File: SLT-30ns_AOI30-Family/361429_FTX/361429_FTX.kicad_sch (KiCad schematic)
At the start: 5 parts, among them T1 IBM_Transistor, T2 IBM_Transistor, T3 IBM_Transistor, T4 IBM_Transistor, U1 12-Pin_SLx_Can

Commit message: Bunch of schematics.
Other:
- note added: "All Transistors ACA"
- note removed: "All Transistors DC"
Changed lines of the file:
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@@
     (stroke (width 0) (type default) (color 0 0 0 0))
   )
-  (text "All Transistors DC" (at 118.11 101.6 0)
+  (text "All Transistors ACA" (at 118.11 101.6 0)
     (effects (font (size 1.27 1.27)) (justify left bottom))
   )
@@
     (pin "3")
   )
+  (symbol (lib_id "IBM_SLT-SLD:IBM_Transistor") (at 165.1 128.27 0) (unit 1)
+    (in_bom yes) (on_board yes) (fields_autoplaced)
+    (property "Reference" "T3" (id 0) (at 168.91 127.6349 0)
+      (effects (font (size 1.27 1.27)) (justify left))
+    )
+    (property "Value" "IBM_Transistor" (id 1) (at 168.91 130.1749 0)
+      (effects (font (size 1.27 1.27)) (justify left))
+    )
+    (property "Footprint" "" (id 2) (at 165.1 128.27 0)
+      (effects (font (size 1.27 1.27)) hide)
+    )
+    (property "Datasheet" "" (id 3) (at 165.1 128.27 0)
+      (effects (font (size 1.27 1.27)) hide)
+    )
+    (pin "1")
+    (pin "2")
+    (pin "3")
+  )
   (symbol (lib_id "IBM_SLT-SLD:12-Pin_SLx_Can") (at 237.49 133.35 0) (unit 1)
     (in_bom yes) (on_board yes) (fields_autoplaced)
@@
     (pin "9")
   )
+  (symbol (lib_id "IBM_SLT-SLD:IBM_Transistor") (at 88.9 73.66 0) (unit 1)
+    (in_bom yes) (on_board yes) (fields_autoplaced)
+    (property "Reference" "T2" (id 0) (at 92.71 73.0249 0)
+      (effects (font (size 1.27 1.27)) (justify left))
+    )
+    (property "Value" "IBM_Transistor" (id 1) (at 92.71 75.5649 0)
+      (effects (font (size 1.27 1.27)) (justify left))
+    )
+    (property "Footprint" "" (id 2) (at 88.9 73.66 0)
+      (effects (font (size 1.27 1.27)) hide)
+    )
+    (property "Datasheet" "" (id 3) (at 88.9 73.66 0)
+      (effects (font (size 1.27 1.27)) hide)
+    )
+    (pin "1")
+    (pin "2")
+    (pin "3")
+  )
   (symbol (lib_id "IBM_SLT-SLD:IBM_Transistor") (at 165.1 73.66 0) (unit 1)
     (in_bom yes) (on_board yes) (fields_autoplaced)
@@
     (pin "3")
   )
-  (symbol (lib_id "IBM_SLT-SLD:IBM_Transistor") (at 88.9 73.66 0) (unit 1)
-    (in_bom yes) (on_board yes) (fields_autoplaced)
-    (property "Reference" "T2" (id 0) (at 92.71 73.0249 0)
-      (effects (font (size 1.27 1.27)) (justify left))
-    )
-    (property "Value" "IBM_Transistor" (id 1) (at 92.71 75.5649 0)
-      (effects (font (size 1.27 1.27)) (justify left))
-    )
-    (property "Footprint" "" (id 2) (at 88.9 73.66 0)
-      (effects (font (size 1.27 1.27)) hide)
-    )
-    (property "Datasheet" "" (id 3) (at 88.9 73.66 0)
-      (effects (font (size 1.27 1.27)) hide)
-    )
-    (pin "1")
-    (pin "2")
-    (pin "3")
-  )
-  (symbol (lib_id "IBM_SLT-SLD:IBM_Transistor") (at 165.1 128.27 0) (unit 1)
-    (in_bom yes) (on_board yes) (fields_autoplaced)
-    (property "Reference" "T3" (id 0) (at 168.91 127.6349 0)
-      (effects (font (size 1.27 1.27)) (justify left))
-    )
-    (property "Value" "IBM_Transistor" (id 1) (at 168.91 130.1749 0)
-      (effects (font (size 1.27 1.27)) (justify left))
-    )
-    (property "Footprint" "" (id 2) (at 165.1 128.27 0)
-      (effects (font (size 1.27 1.27)) hide)
-    )
-    (property "Datasheet" "" (id 3) (at 165.1 128.27 0)
-      (effects (font (size 1.27 1.27)) hide)
-    )
-    (pin "1")
-    (pin "2")
-    (pin "3")
-  )
   (sheet_instances
     (path "/" (page "1"))
   )
   (symbol_instances
-    (path "/1f8e8439-29d6-48dc-85a2-31fc4a1324d9"
+    (path "/2137906f-9d9a-4f2a-b4c3-18311f4a4bdf"
       (reference "T1") (unit 1) (value "IBM_Transistor") (footprint "")
     )
-    (path "/89093827-bb23-4e39-8ebb-d4aae8eed604"
+    (path "/c36f7147-bc6f-4cbe-8b56-617ae1aaead3"
       (reference "T2") (unit 1) (value "IBM_Transistor") (footprint "")
     )
-    (path "/fc223558-0a2b-4b0e-b949-b7fb185c9d35"
+    (path "/313d7939-b1f4-4f95-8fbf-38d2d1bd0a6a"
       (reference "T3") (unit 1) (value "IBM_Transistor") (footprint "")
     )
-    (path "/80f5072b-6b7f-47f8-a9c1-14d05fac811f"
+    (path "/d1e37067-05b9-4eaf-979b-bfe29351874a"
       (reference "T4") (unit 1) (value "IBM_Transistor") (footprint "")
     )

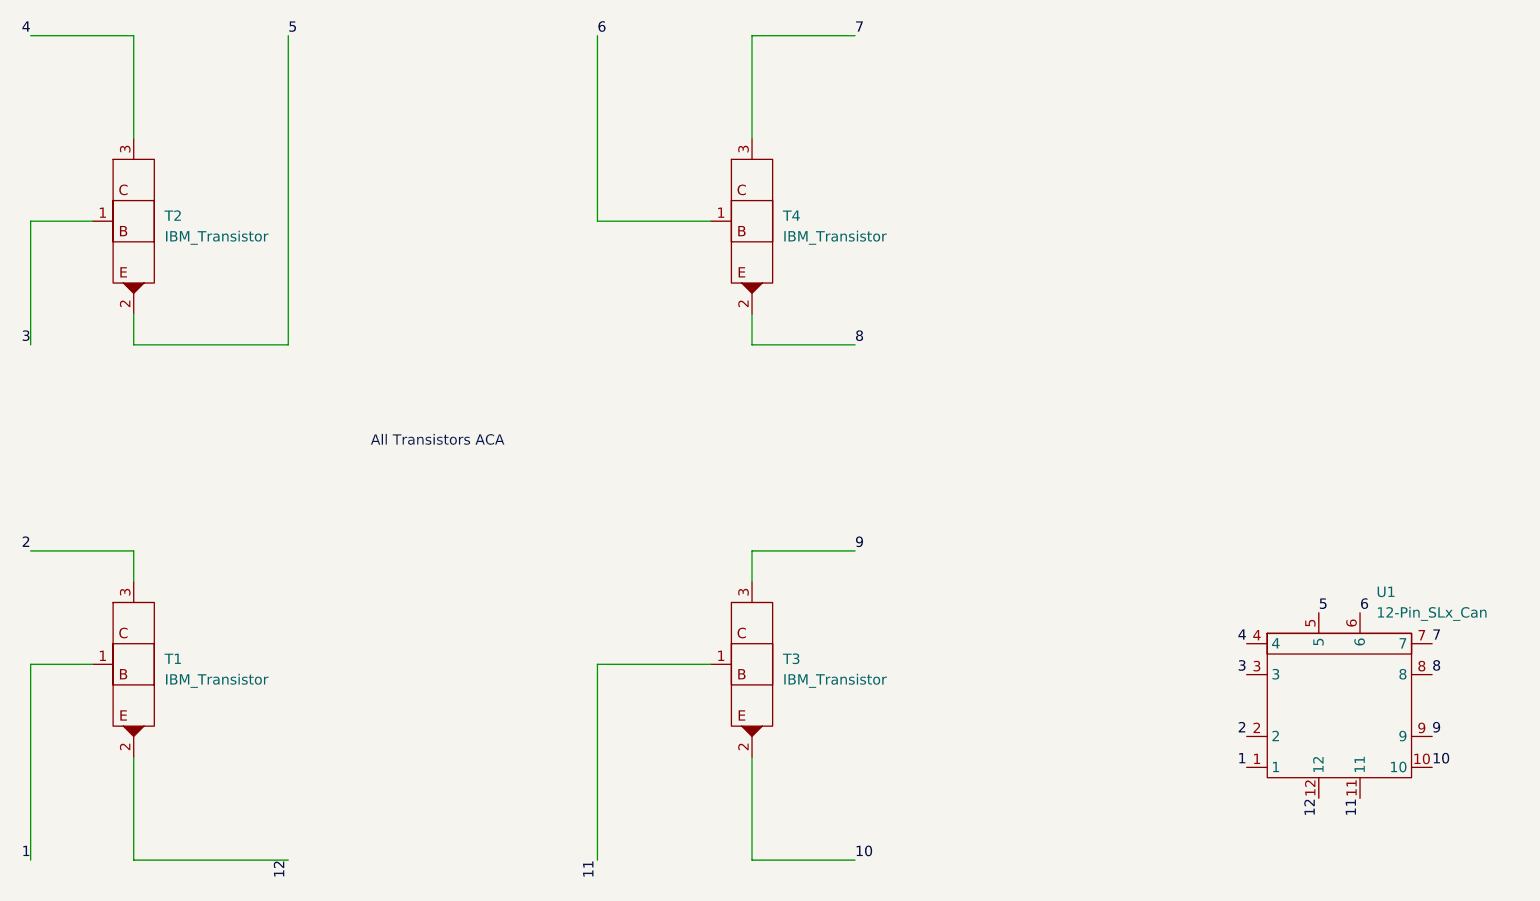
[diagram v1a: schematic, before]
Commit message: Finished off the SLT-30 family of parts, started on the SLT-700 family. Changed labeling of transistors and diodes in all schematics, but have yet to update all the pdf files. This is a TODO...
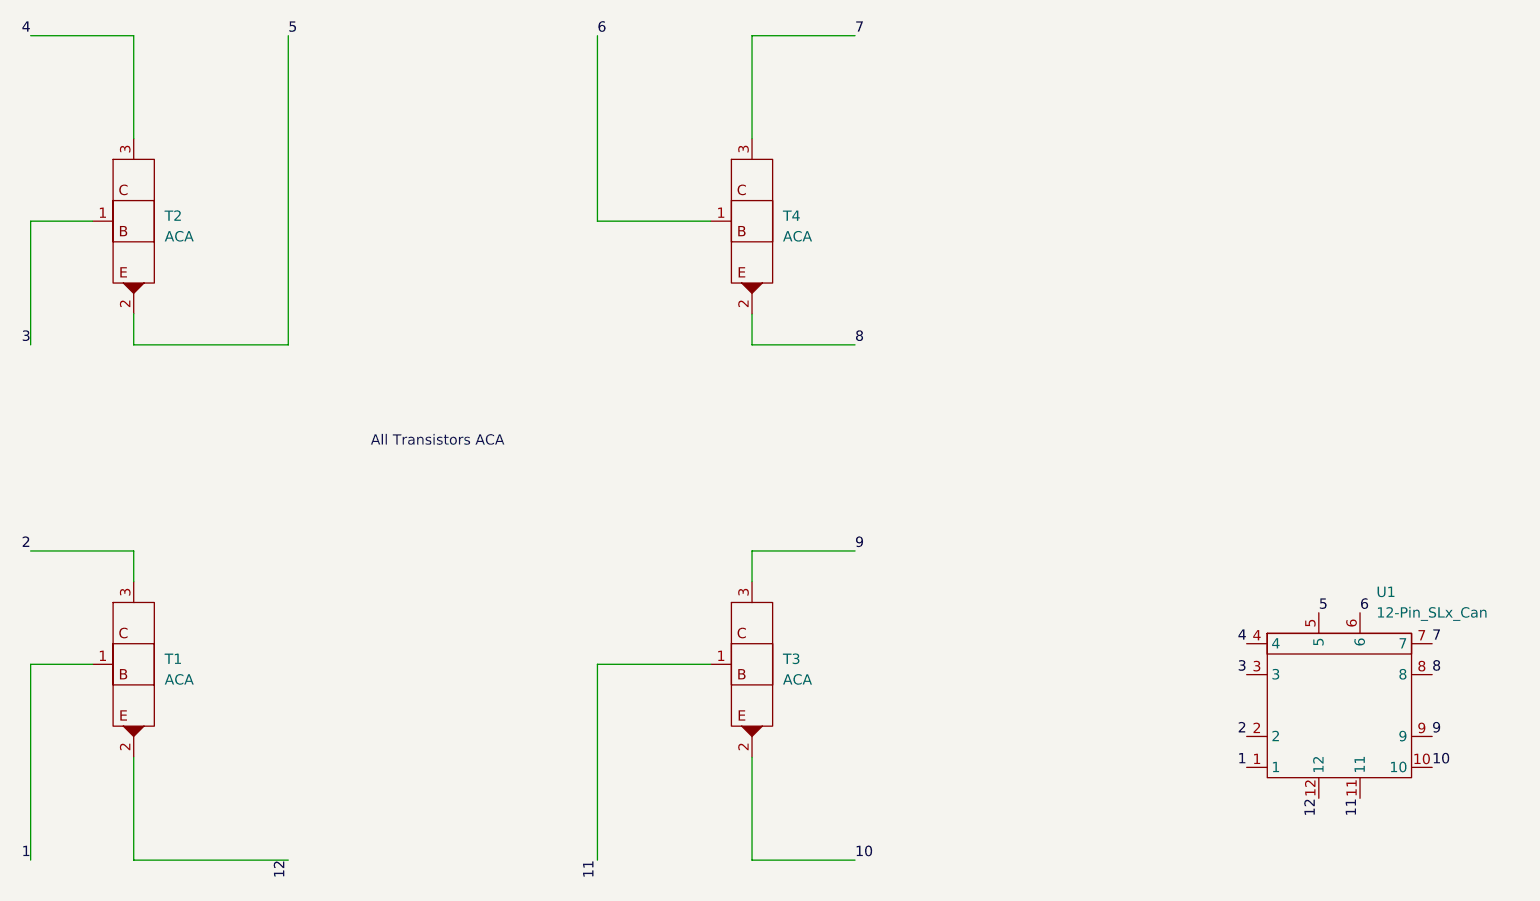
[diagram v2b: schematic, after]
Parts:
- T1, T2, T3, T4: value IBM_Transistor -> ACA
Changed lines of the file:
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@@
       (effects (font (size 1.27 1.27)) (justify left))
     )
-    (property "Value" "IBM_Transistor" (id 1) (at 92.71 130.1749 0)
+    (property "Value" "ACA" (id 1) (at 92.71 130.1749 0)
       (effects (font (size 1.27 1.27)) (justify left))
     )
@@
       (effects (font (size 1.27 1.27)) (justify left))
     )
-    (property "Value" "IBM_Transistor" (id 1) (at 168.91 130.1749 0)
+    (property "Value" "ACA" (id 1) (at 168.91 130.1749 0)
       (effects (font (size 1.27 1.27)) (justify left))
     )
@@
       (effects (font (size 1.27 1.27)) (justify left))
     )
-    (property "Value" "IBM_Transistor" (id 1) (at 92.71 75.5649 0)
+    (property "Value" "ACA" (id 1) (at 92.71 75.5649 0)
       (effects (font (size 1.27 1.27)) (justify left))
     )
@@
       (effects (font (size 1.27 1.27)) (justify left))
     )
-    (property "Value" "IBM_Transistor" (id 1) (at 168.91 75.5649 0)
+    (property "Value" "ACA" (id 1) (at 168.91 75.5649 0)
       (effects (font (size 1.27 1.27)) (justify left))
     )
@@
   (symbol_instances
     (path "/2137906f-9d9a-4f2a-b4c3-18311f4a4bdf"
-      (reference "T1") (unit 1) (value "IBM_Transistor") (footprint "")
+      (reference "T1") (unit 1) (value "ACA") (footprint "")
     )
     (path "/c36f7147-bc6f-4cbe-8b56-617ae1aaead3"
-      (reference "T2") (unit 1) (value "IBM_Transistor") (footprint "")
+      (reference "T2") (unit 1) (value "ACA") (footprint "")
     )
     (path "/313d7939-b1f4-4f95-8fbf-38d2d1bd0a6a"
-      (reference "T3") (unit 1) (value "IBM_Transistor") (footprint "")
+      (reference "T3") (unit 1) (value "ACA") (footprint "")
     )
     (path "/d1e37067-05b9-4eaf-979b-bfe29351874a"
-      (reference "T4") (unit 1) (value "IBM_Transistor") (footprint "")
+      (reference "T4") (unit 1) (value "ACA") (footprint "")
     )
     (path "/75e072b9-86c1-407b-a1c4-16b7a7044004"

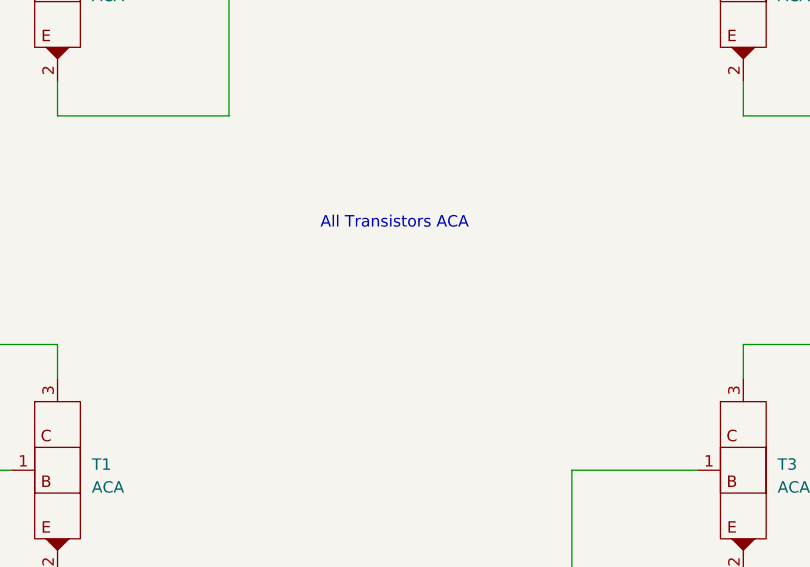
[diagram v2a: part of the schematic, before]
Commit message: Update schematic pdfs
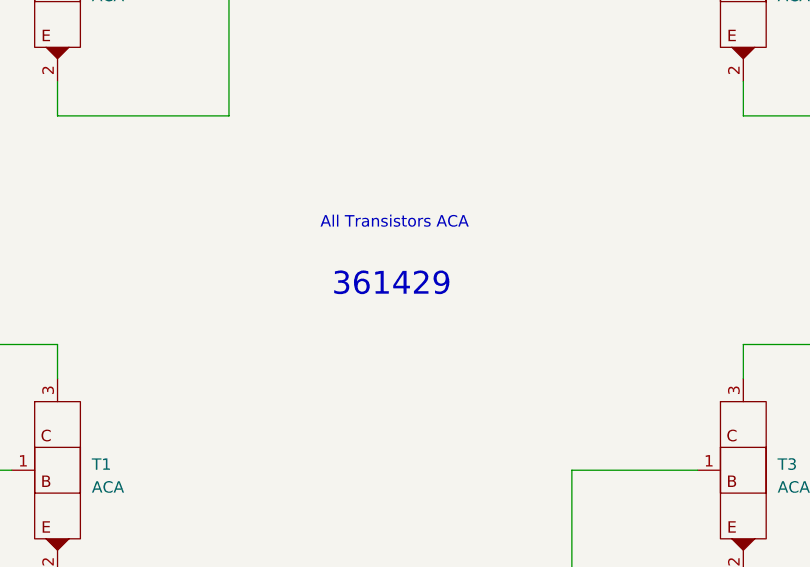
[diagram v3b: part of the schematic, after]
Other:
- note added: "361429"
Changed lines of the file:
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@@
     (stroke (width 0) (type default) (color 0 0 0 0))
+  )
+  (text "361429" (at 119.38 109.22 0)
+    (effects (font (size 2.54 2.54)) (justify left bottom))
   )
   (text "All Transistors ACA" (at 118.11 101.6 0)
